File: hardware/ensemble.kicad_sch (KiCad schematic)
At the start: 22 parts, among them J1 E1, SW1 4PDT Toggle, SW2 SPDT Toggle, SW3 SPST, T1 42TM_XX, U1 LM741

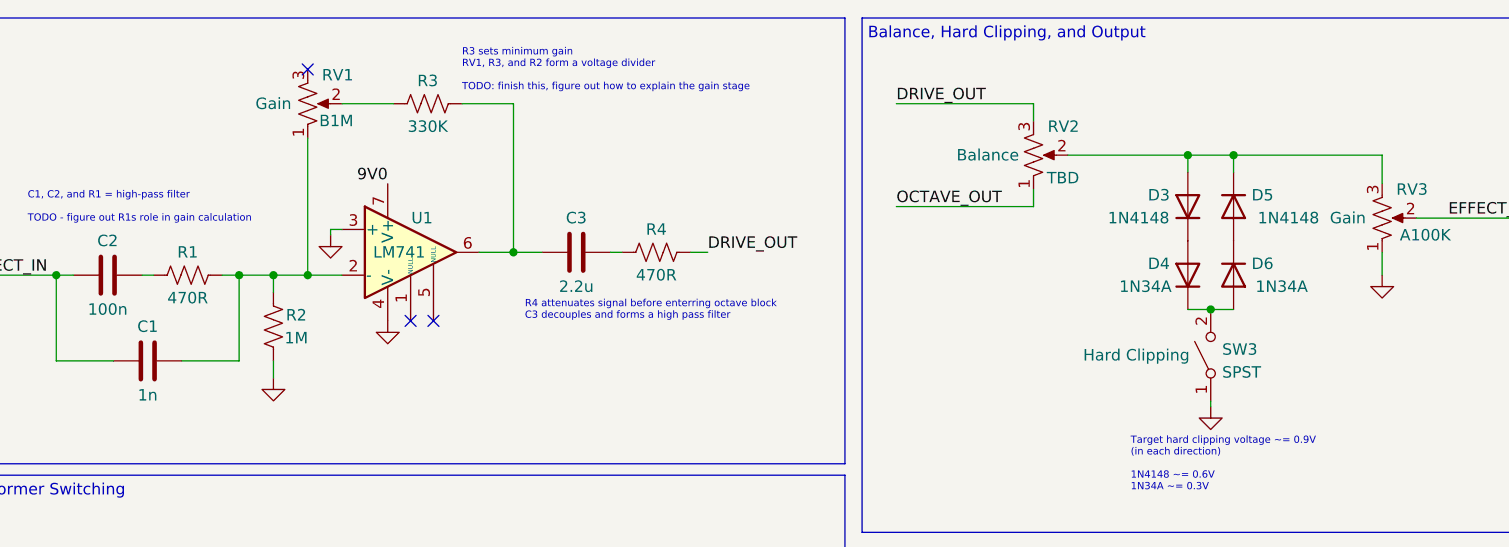
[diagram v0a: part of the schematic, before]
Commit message: add footprints and models for all components
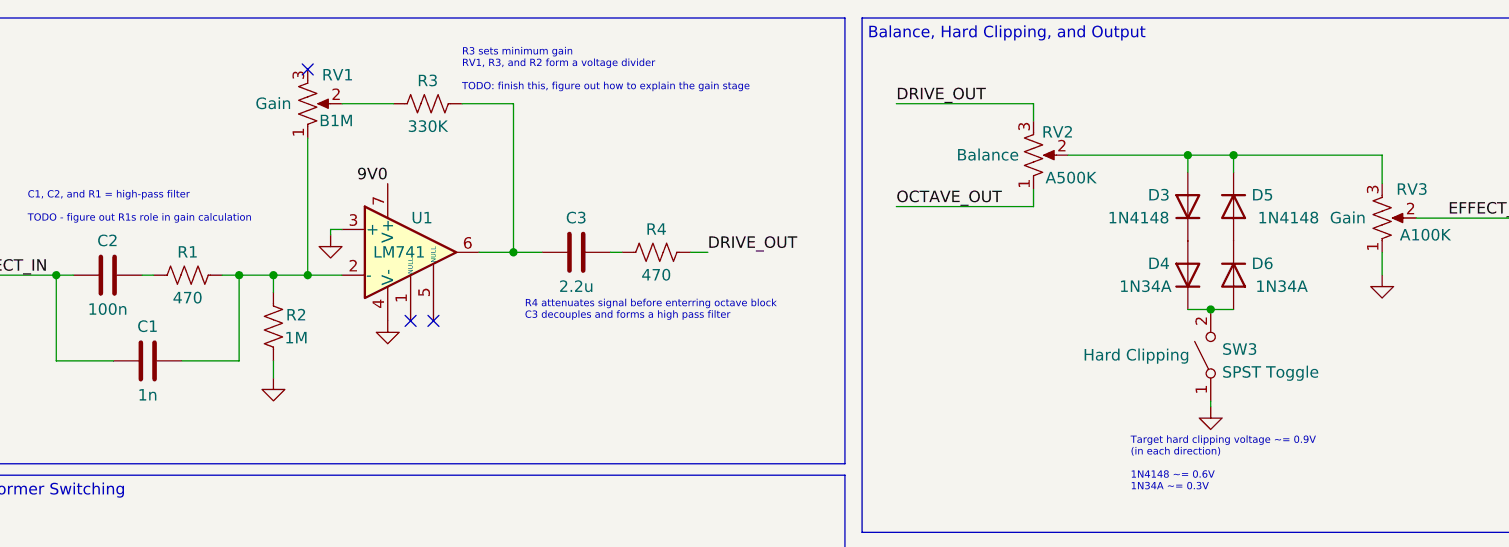
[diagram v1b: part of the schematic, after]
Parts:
- C1, C2, C3: footprint (none) -> Capacitor_THT:C_Rect_L7.2mm_W2.5mm_P5.00mm_FKS2_FKP2_MKS2_MKP2
- D1, D2, D3, D4, D5, D6: footprint (none) -> Diode_THT:D_DO-34_SOD68_P7.62mm_Horizontal
- J1: footprint random_input:Molex_PicoBlade_53047-0410_1x04_P1.25mm_Vertical_with_3D_Model -> ensemble:Molex_PicoBlade_53047-0410_1x04_P1.25mm_Vertical_with_3D_Model
- R1, R4: value 470R -> 470; footprint (none) -> Resistor_THT:R_Axial_DIN0207_L6.3mm_D2.5mm_P7.62mm_Horizontal
- R2, R3: footprint (none) -> Resistor_THT:R_Axial_DIN0207_L6.3mm_D2.5mm_P7.62mm_Horizontal
- RV1, RV3: footprint (none) -> ensemble:Potentiometer_Single_3_Horizontal
- RV2: value TBD -> A500K; footprint (none) -> ensemble:Potentiometer_Single_3_Horizontal
- SW1: footprint (none) -> ensemble:SW_4PDT_SOLDER_LUGS
- SW2: footprint (none) -> ensemble:SW_SPDT_SOLDER_LUGS
- SW3: value SPST -> SPST Toggle; footprint (none) -> ensemble:SW_SPDT_SOLDER_LUGS
- T1: footprint (none) -> ensemble:Transformer_42TM
- U1: footprint (none) -> Package_DIP:DIP-8_W7.62mm_Socket
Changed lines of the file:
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@@
       (effects (font (size 1.27 1.27)) hide)
     )
-    (property "Footprint" "" (at 53.34 86.995 0)
+    (property "Footprint" "ensemble:SW_4PDT_SOLDER_LUGS" (at 53.34 86.995 0)
       (effects (font (size 1.27 1.27)) hide)
     )
@@
       (effects (font (size 1.27 1.27)))
     )
-    (property "Footprint" "" (at 83.185 128.905 0)
+    (property "Footprint" "Diode_THT:D_DO-34_SOD68_P7.62mm_Horizontal" (at 83.185 128.905 0)
       (effects (font (size 1.27 1.27)) hide)
     )
@@
       (effects (font (size 1.27 1.27)) (justify right))
     )
-    (property "Footprint" "" (at 172.72 34.925 0)
+    (property "Footprint" "ensemble:Potentiometer_Single_3_Horizontal" (at 172.72 34.925 0)
       (effects (font (size 1.27 1.27)) hide)
     )
@@
   (symbol (lib_id "Device:R_Potentiometer_US") (at 133.985 27.94 0) (mirror x) (unit 1)
     (in_bom yes) (on_board yes) (dnp no)
-    (property "Reference" "RV2" (at 139.065 24.765 0)
-      (effects (font (size 1.27 1.27)) (justify right))
-    )
-    (property "Value" "TBD" (at 139.065 30.48 0)
-      (effects (font (size 1.27 1.27)) (justify right))
-    )
-    (property "Footprint" "" (at 133.985 27.94 0)
+    (property "Reference" "RV2" (at 138.43 25.4 0)
+      (effects (font (size 1.27 1.27)) (justify right))
+    )
+    (property "Value" "A500K" (at 140.97 30.48 0)
+      (effects (font (size 1.27 1.27)) (justify right))
+    )
+    (property "Footprint" "ensemble:Potentiometer_Single_3_Horizontal" (at 133.985 27.94 0)
       (effects (font (size 1.27 1.27)) hide)
     )
@@
       (effects (font (size 1.27 1.27)) (justify right))
     )
-    (property "Footprint" "" (at 156.21 33.655 0)
+    (property "Footprint" "Diode_THT:D_DO-34_SOD68_P7.62mm_Horizontal" (at 156.21 33.655 0)
       (effects (font (size 1.27 1.27)) hide)
     )
@@
       (effects (font (size 1.27 1.27)))
     )
-    (property "Footprint" "" (at 38.735 131.445 0)
+    (property "Footprint" "ensemble:Transformer_42TM" (at 38.735 131.445 0)
       (effects (font (size 1.27 1.27)) hide)
     )
@@
       (effects (font (size 1.27 1.27)))
     )
-    (property "Footprint" "" (at 86.995 37.7698 0)
+    (property "Footprint" "Capacitor_THT:C_Rect_L7.2mm_W2.5mm_P5.00mm_FKS2_FKP2_MKS2_MKP2" (at 86.995 37.7698 0)
       (effects (font (size 1.27 1.27)) hide)
     )
@@
       (effects (font (size 1.27 1.27)))
     )
-    (property "Footprint" "" (at 39.37 49.8348 0)
+    (property "Footprint" "Capacitor_THT:C_Rect_L7.2mm_W2.5mm_P5.00mm_FKS2_FKP2_MKS2_MKP2" (at 39.37 49.8348 0)
       (effects (font (size 1.27 1.27)) hide)
     )
@@
       (effects (font (size 1.27 1.27)))
     )
-    (property "Footprint" "" (at 48.514 46.736 90)
+    (property "Footprint" "Resistor_THT:R_Axial_DIN0207_L6.3mm_D2.5mm_P7.62mm_Horizontal" (at 48.514 46.736 90)
       (effects (font (size 1.27 1.27)) hide)
     )
@@
       (effects (font (size 1.27 1.27)) (justify right))
     )
-    (property "Footprint" "" (at 151.13 41.275 0)
+    (property "Footprint" "Diode_THT:D_DO-34_SOD68_P7.62mm_Horizontal" (at 151.13 41.275 0)
       (effects (font (size 1.27 1.27)) hide)
     )
@@
       (effects (font (size 1.27 1.27)))
     )
-    (property "Footprint" "" (at 28.575 80.645 0)
+    (property "Footprint" "ensemble:SW_4PDT_SOLDER_LUGS" (at 28.575 80.645 0)
       (effects (font (size 1.27 1.27)) hide)
     )
@@
       (effects (font (size 1.27 1.27)))
     )
-    (property "Footprint" "" (at 66.04 37.465 0)
+    (property "Footprint" "Package_DIP:DIP-8_W7.62mm_Socket" (at 66.04 37.465 0)
       (effects (font (size 1.27 1.27)) hide)
     )
@@
       (effects (font (size 1.27 1.27)) (justify right))
     )
-    (property "Footprint" "" (at 156.21 41.275 0)
+    (property "Footprint" "Diode_THT:D_DO-34_SOD68_P7.62mm_Horizontal" (at 156.21 41.275 0)
       (effects (font (size 1.27 1.27)) hide)
     )
@@
       (effects (font (size 1.27 1.27)) hide)
     )
-    (property "Footprint" "" (at 28.575 92.075 0)
+    (property "Footprint" "ensemble:SW_4PDT_SOLDER_LUGS" (at 28.575 92.075 0)
       (effects (font (size 1.27 1.27)) hide)
     )
@@
       (effects (font (size 1.27 1.27)))
     )
-    (property "Value" "470R" (at 40.005 43.815 90)
-      (effects (font (size 1.27 1.27)))
-    )
-    (property "Footprint" "" (at 39.751 42.291 90)
+    (property "Value" "470" (at 40.005 43.815 90)
+      (effects (font (size 1.27 1.27)))
+    )
+    (property "Footprint" "Resistor_THT:R_Axial_DIN0207_L6.3mm_D2.5mm_P7.62mm_Horizontal" (at 39.751 42.291 90)
       (effects (font (size 1.27 1.27)) hide)
     )
@@
       (effects (font (size 1.27 1.27)))
     )
-    (property "Footprint" "" (at 93.345 88.265 0)
+    (property "Footprint" "ensemble:SW_SPDT_SOLDER_LUGS" (at 93.345 88.265 0)
       (effects (font (size 1.27 1.27)) hide)
     )
@@
       (effects (font (size 1.27 1.27)))
     )
-    (property "Footprint" "" (at 34.925 40.3098 0)
+    (property "Footprint" "Capacitor_THT:C_Rect_L7.2mm_W2.5mm_P5.00mm_FKS2_FKP2_MKS2_MKP2" (at 34.925 40.3098 0)
       (effects (font (size 1.27 1.27)) hide)
     )
@@
       (effects (font (size 1.27 1.27)) (justify right))
     )
-    (property "Footprint" "" (at 53.34 22.225 0)
+    (property "Footprint" "ensemble:Potentiometer_Single_3_Horizontal" (at 53.34 22.225 0)
       (effects (font (size 1.27 1.27)) hide)
     )
@@
       (effects (font (size 1.27 1.27)) (justify left))
     )
-    (property "Footprint" "random_input:Molex_PicoBlade_53047-0410_1x04_P1.25mm_Vertical_with_3D_Model" (at 184.15 83.185 0)
+    (property "Footprint" "ensemble:Molex_PicoBlade_53047-0410_1x04_P1.25mm_Vertical_with_3D_Model" (at 184.15 83.185 0)
       (effects (font (size 1.27 1.27)) hide)
     )
@@
       (effects (font (size 1.27 1.27)))
     )
-    (property "Footprint" "" (at 83.185 118.745 0)
+    (property "Footprint" "Diode_THT:D_DO-34_SOD68_P7.62mm_Horizontal" (at 83.185 118.745 0)
       (effects (font (size 1.27 1.27)) hide)
     )
@@
       (effects (font (size 1.27 1.27)) (justify right))
     )
-    (property "Footprint" "" (at 151.13 33.655 0)
+    (property "Footprint" "Diode_THT:D_DO-34_SOD68_P7.62mm_Horizontal" (at 151.13 33.655 0)
       (effects (font (size 1.27 1.27)) hide)
     )
@@
       (effects (font (size 1.27 1.27)) hide)
     )
-    (property "Footprint" "" (at 53.34 75.565 0)
+    (property "Footprint" "ensemble:SW_4PDT_SOLDER_LUGS" (at 53.34 75.565 0)
       (effects (font (size 1.27 1.27)) hide)
     )
@@
       (effects (font (size 1.27 1.27)) (justify right))
     )
-    (property "Value" "SPST" (at 154.94 52.07 90)
-      (effects (font (size 1.27 1.27)) (justify right))
-    )
-    (property "Footprint" "" (at 153.67 50.165 0)
+    (property "Value" "SPST Toggle" (at 154.94 52.07 90)
+      (effects (font (size 1.27 1.27)) (justify right))
+    )
+    (property "Footprint" "ensemble:SW_SPDT_SOLDER_LUGS" (at 153.67 50.165 0)
       (effects (font (size 1.27 1.27)) hide)
     )
@@
       (effects (font (size 1.27 1.27)))
     )
-    (property "Value" "470R" (at 92.075 41.275 90)
-      (effects (font (size 1.27 1.27)))
-    )
-    (property "Footprint" "" (at 91.821 39.751 90)
+    (property "Value" "470" (at 92.075 41.275 90)
+      (effects (font (size 1.27 1.27)))
+    )
+    (property "Footprint" "Resistor_THT:R_Axial_DIN0207_L6.3mm_D2.5mm_P7.62mm_Horizontal" (at 91.821 39.751 90)
       (effects (font (size 1.27 1.27)) hide)
     )
@@
       (effects (font (size 1.27 1.27)))
     )
-    (property "Footprint" "" (at 66.929 21.209 90)
-      (effects (font (size 1.27 1.27)) hide)
-    )
+    (property "Footprint" "Resistor_THT:R_Axial_DIN0207_L6.3mm_D2.5mm_P7.62mm_Horizontal" (at 66.929 21.209 90)
+      (effects (font (size 1.27 1.27)) hide)
+    )

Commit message: initial layout
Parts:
- C3: value 2.2u -> 2u2
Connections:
- net GND: now also SW1.8 (C2); no longer SW1.5 (B2)
- net RECT_TOP: now also SW1.5 (B2); no longer SW1.8 (C2)
- net XFM_P1: now also SW1.4 (B1); no longer SW1.7 (C1)
- net XFM_P3: now also SW1.9 (C3); no longer SW1.6 (B3)
- net XFM_S1: now also SW1.6 (B3); no longer SW1.9 (C3)
- net XFM_S3: now also SW1.7 (C1); no longer SW1.4 (B1)
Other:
- moved on the sheet: SW1B, SW1C

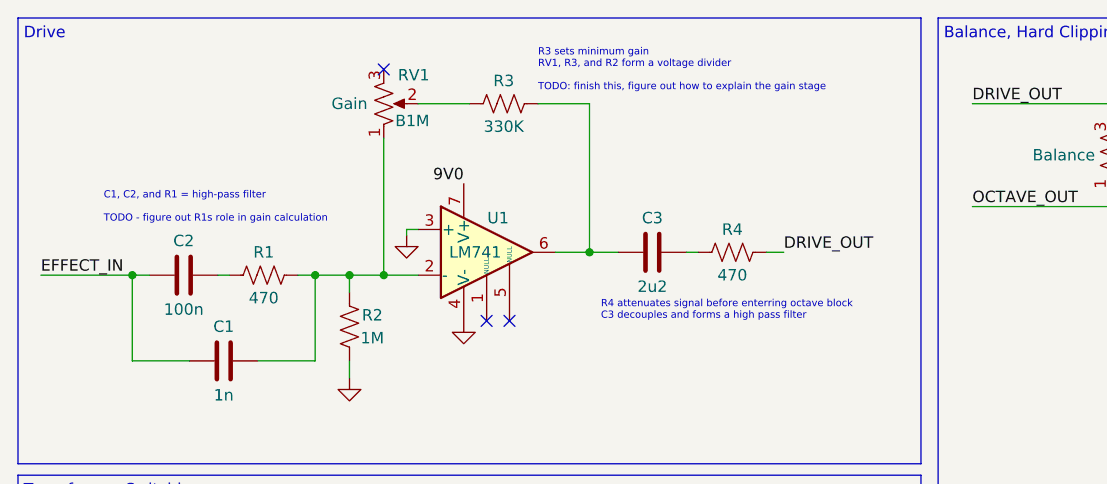
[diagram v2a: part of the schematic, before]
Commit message: tweak input-side filtering based on simulations, move to correct footprint for caps and diodes.
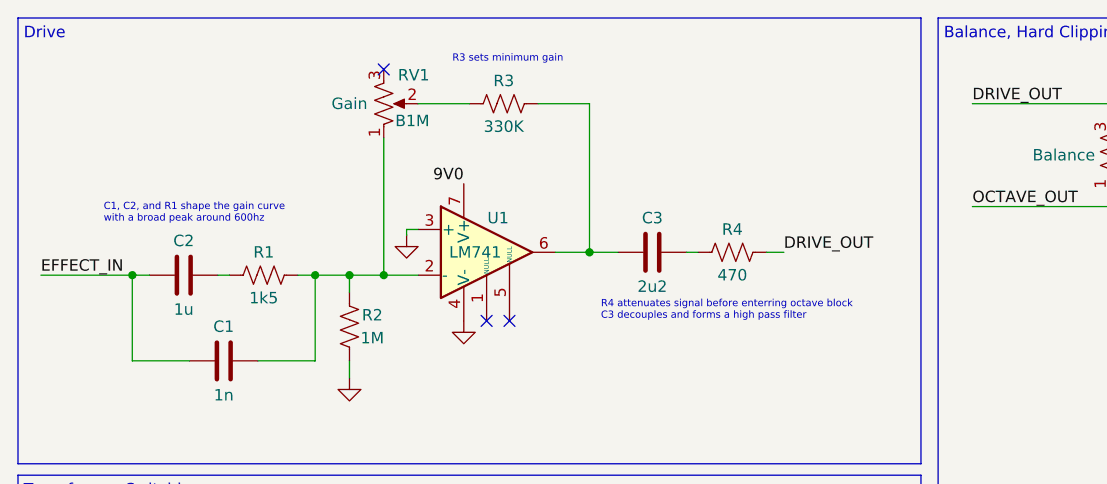
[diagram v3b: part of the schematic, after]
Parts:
- C1, C3: footprint Capacitor_THT:C_Rect_L7.2mm_W2.5mm_P5.00mm_FKS2_FKP2_MKS2_MKP2 -> Capacitor_THT:C_Disc_D4.3mm_W1.9mm_P5.00mm
- C2: value 100n -> 1u; footprint Capacitor_THT:C_Rect_L7.2mm_W2.5mm_P5.00mm_FKS2_FKP2_MKS2_MKP2 -> Capacitor_THT:C_Disc_D4.3mm_W1.9mm_P5.00mm
- D1, D2, D3, D4, D5, D6: footprint Diode_THT:D_DO-34_SOD68_P7.62mm_Horizontal -> Diode_THT:D_DO-35_SOD27_P7.62mm_Horizontal
- R1: value 470 -> 1k5
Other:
- note added: "C1, C2, and R1 shape the gain curve with a broad peak around 600hz"
- note added: "R3 sets minimum gain"
- note removed: "C1, C2, and R1 = high-pass filter TODO - figure out R1s role in gain calculation"
- note removed: "R3 sets minimum gain RV1, R3, and R2 form a voltage divider TODO: finish this, figure out how to explain the gain stage"
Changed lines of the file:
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@@
   (title_block
     (title "Ensemble fuzz effect")
-    (date "2023-03-17")
-    (rev "v0.01")
+    (date "2023-03-19")
+    (rev "v0.02")
     (comment 1 "github.com/whbeers/ensemble")
   )
@@
     (effects (font (size 1.27 1.27)) (justify left bottom))
   )
-  (text "C1, C2, and R1 = high-pass filter\n\nTODO - figure out R1s role in gain calculation"
+  (text "C1, C2, and R1 shape the gain curve\nwith a broad peak around 600hz"
     (at 22.225 35.56 0)
     (effects (font (size 0.8 0.8)) (justify left bottom))
@@
     (effects (font (size 1.27 1.27)) (justify left bottom))
   )
-  (text "R3 sets minimum gain\nRV1, R3, and R2 form a voltage divider\n\nTODO: finish this, figure out how to explain the gain stage"
-    (at 70.485 20.955 0)
+  (text "R3 sets minimum gain" (at 60.96 17.78 0)
     (effects (font (size 0.8 0.8)) (justify left bottom))
   )
@@
       (effects (font (size 1.27 1.27)))
     )
-    (property "Footprint" "Diode_THT:D_DO-34_SOD68_P7.62mm_Horizontal" (at 83.185 128.905 0)
+    (property "Footprint" "Diode_THT:D_DO-35_SOD27_P7.62mm_Horizontal" (at 83.185 128.905 0)
       (effects (font (size 1.27 1.27)) hide)
     )
@@
       (effects (font (size 1.27 1.27)) (justify right))
     )
-    (property "Footprint" "Diode_THT:D_DO-34_SOD68_P7.62mm_Horizontal" (at 156.21 33.655 0)
+    (property "Footprint" "Diode_THT:D_DO-35_SOD27_P7.62mm_Horizontal" (at 156.21 33.655 0)
       (effects (font (size 1.27 1.27)) hide)
     )
@@
       (effects (font (size 1.27 1.27)))
     )
-    (property "Footprint" "Capacitor_THT:C_Rect_L7.2mm_W2.5mm_P5.00mm_FKS2_FKP2_MKS2_MKP2" (at 86.995 37.7698 0)
+    (property "Footprint" "Capacitor_THT:C_Disc_D4.3mm_W1.9mm_P5.00mm" (at 86.995 37.7698 0)
       (effects (font (size 1.27 1.27)) hide)
     )
@@
       (effects (font (size 1.27 1.27)))
     )
-    (property "Footprint" "Capacitor_THT:C_Rect_L7.2mm_W2.5mm_P5.00mm_FKS2_FKP2_MKS2_MKP2" (at 39.37 49.8348 0)
+    (property "Footprint" "Capacitor_THT:C_Disc_D4.3mm_W1.9mm_P5.00mm" (at 39.37 49.8348 0)
       (effects (font (size 1.27 1.27)) hide)
     )
@@
       (effects (font (size 1.27 1.27)) (justify right))
     )
-    (property "Footprint" "Diode_THT:D_DO-34_SOD68_P7.62mm_Horizontal" (at 151.13 41.275 0)
+    (property "Footprint" "Diode_THT:D_DO-35_SOD27_P7.62mm_Horizontal" (at 151.13 41.275 0)
       (effects (font (size 1.27 1.27)) hide)
     )
@@
       (effects (font (size 1.27 1.27)) (justify right))
     )
-    (property "Footprint" "Diode_THT:D_DO-34_SOD68_P7.62mm_Horizontal" (at 156.21 41.275 0)
+    (property "Footprint" "Diode_THT:D_DO-35_SOD27_P7.62mm_Horizontal" (at 156.21 41.275 0)
       (effects (font (size 1.27 1.27)) hide)
     )
@@
       (effects (font (size 1.27 1.27)))
     )
-    (property "Value" "470" (at 40.005 43.815 90)
+    (property "Value" "1k5" (at 40.005 43.815 90)
       (effects (font (size 1.27 1.27)))
     )
@@
       (effects (font (size 1.27 1.27)))
     )
-    (property "Value" "100n" (at 31.115 45.085 90)
-      (effects (font (size 1.27 1.27)))
-    )
-    (property "Footprint" "Capacitor_THT:C_Rect_L7.2mm_W2.5mm_P5.00mm_FKS2_FKP2_MKS2_MKP2" (at 34.925 40.3098 0)
+    (property "Value" "1u" (at 31.115 45.085 90)
+      (effects (font (size 1.27 1.27)))
+    )
+    (property "Footprint" "Capacitor_THT:C_Disc_D4.3mm_W1.9mm_P5.00mm" (at 34.925 40.3098 0)
       (effects (font (size 1.27 1.27)) hide)
     )
@@
       (effects (font (size 1.27 1.27)))
     )
-    (property "Footprint" "Diode_THT:D_DO-34_SOD68_P7.62mm_Horizontal" (at 83.185 118.745 0)
+    (property "Footprint" "Diode_THT:D_DO-35_SOD27_P7.62mm_Horizontal" (at 83.185 118.745 0)
       (effects (font (size 1.27 1.27)) hide)
     )
@@
       (effects (font (size 1.27 1.27)) (justify right))
     )
-    (property "Footprint" "Diode_THT:D_DO-34_SOD68_P7.62mm_Horizontal" (at 151.13 33.655 0)
-      (effects (font (size 1.27 1.27)) hide)
-    )
+    (property "Footprint" "Diode_THT:D_DO-35_SOD27_P7.62mm_Horizontal" (at 151.13 33.655 0)
+      (effects (font (size 1.27 1.27)) hide)
+    )
